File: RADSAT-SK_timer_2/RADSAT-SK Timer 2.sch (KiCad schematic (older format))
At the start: 54 parts, among them J201 Conn_01x07, J202 Conn_01x05_Female, J203 Conn_01x03, J204 Conn_01x02, J205 Conn_01x02, J206 Conn_01x02, J207 Conn_02x26_Odd_Even, J208 Conn_02x26_Odd_Even, J209 Conn_01x15, Q101 IRLML2060, Q102 IRLML2060, Q103 IRLML2060, SW201 SW_Push, SW202 SW_Push, SW203 SW_Push, SW204 SW_Push, SW205 SW_Push, SW206 SW_Push, U101 LT1521IS8-5TR, U202 TPS3700DDCR, U230 CPC1114N, U240 CPC1114N, U250 CPC1114N, U260 CPC1114N

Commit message: added test points
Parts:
- removed J209: Conn_01x15, Connector_Hirose:Hirose_DF13-15P-1.25DSA_1x15_P1.25mm_Vertical, symbol Connector_Generic:Conn_01x15
- added TP101, TP102, TP103, TP104, TP105, TP106, TP107, TP108, TP109, TP110, TP111, TP112, TP113, TP114, TP115, TP116: TestPoint, S2761-46R:HARWIN_S2761-46R, symbol Connector:TestPoint
- C103: value C -> 10uF
- R103: value R -> 1k
- R104: value R -> 2k
- renumbered Q101 to Q204, Q103 to Q205, Q102 to Q206
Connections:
- net labels removed: Test_CHRG_ON-OFF, Test_CSKB_3V3, Test_CSKB_5V, Test_GND, Test_I2C_CLK, Test_I2C_DATA, Test_INA+, Test_INB-, Test_InhibV+, Test_Relay_Inhibs, Test_SW1, Test_SW2, Test_USB_Charge, Test_Vreg, Test_negetive_Batt
- wire segments 185 -> 194

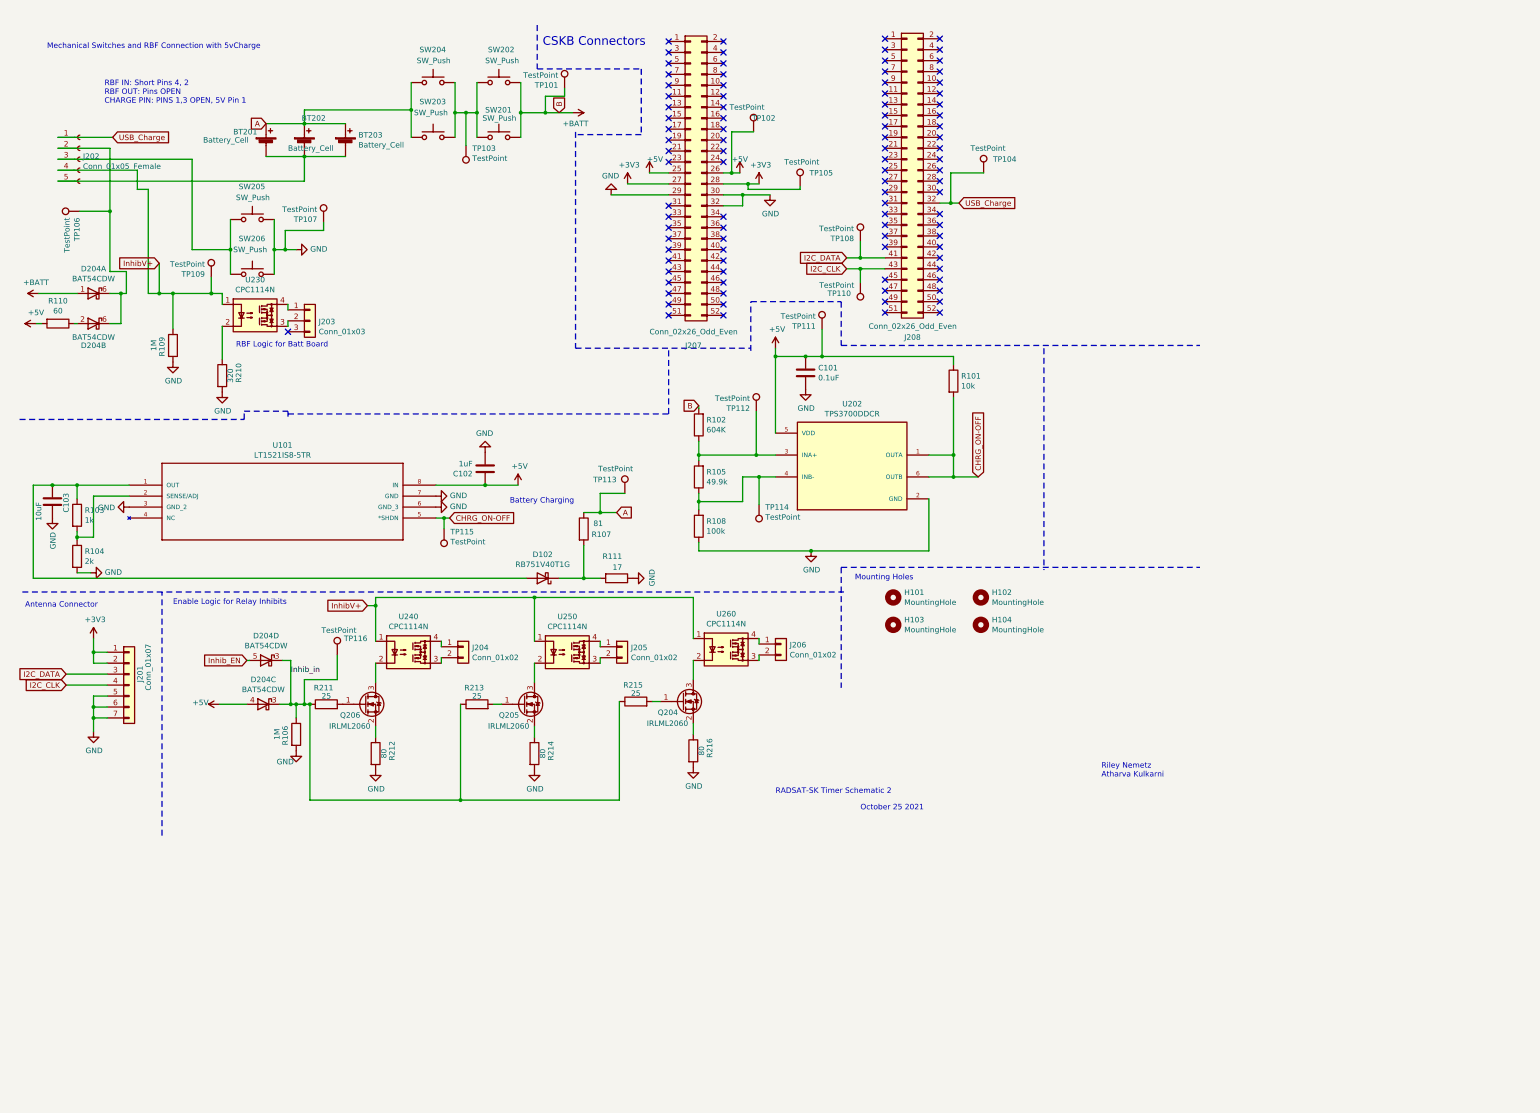
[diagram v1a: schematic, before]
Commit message: added galaxia timer in schematic, made footprint for galaxia timer and added to PCB new
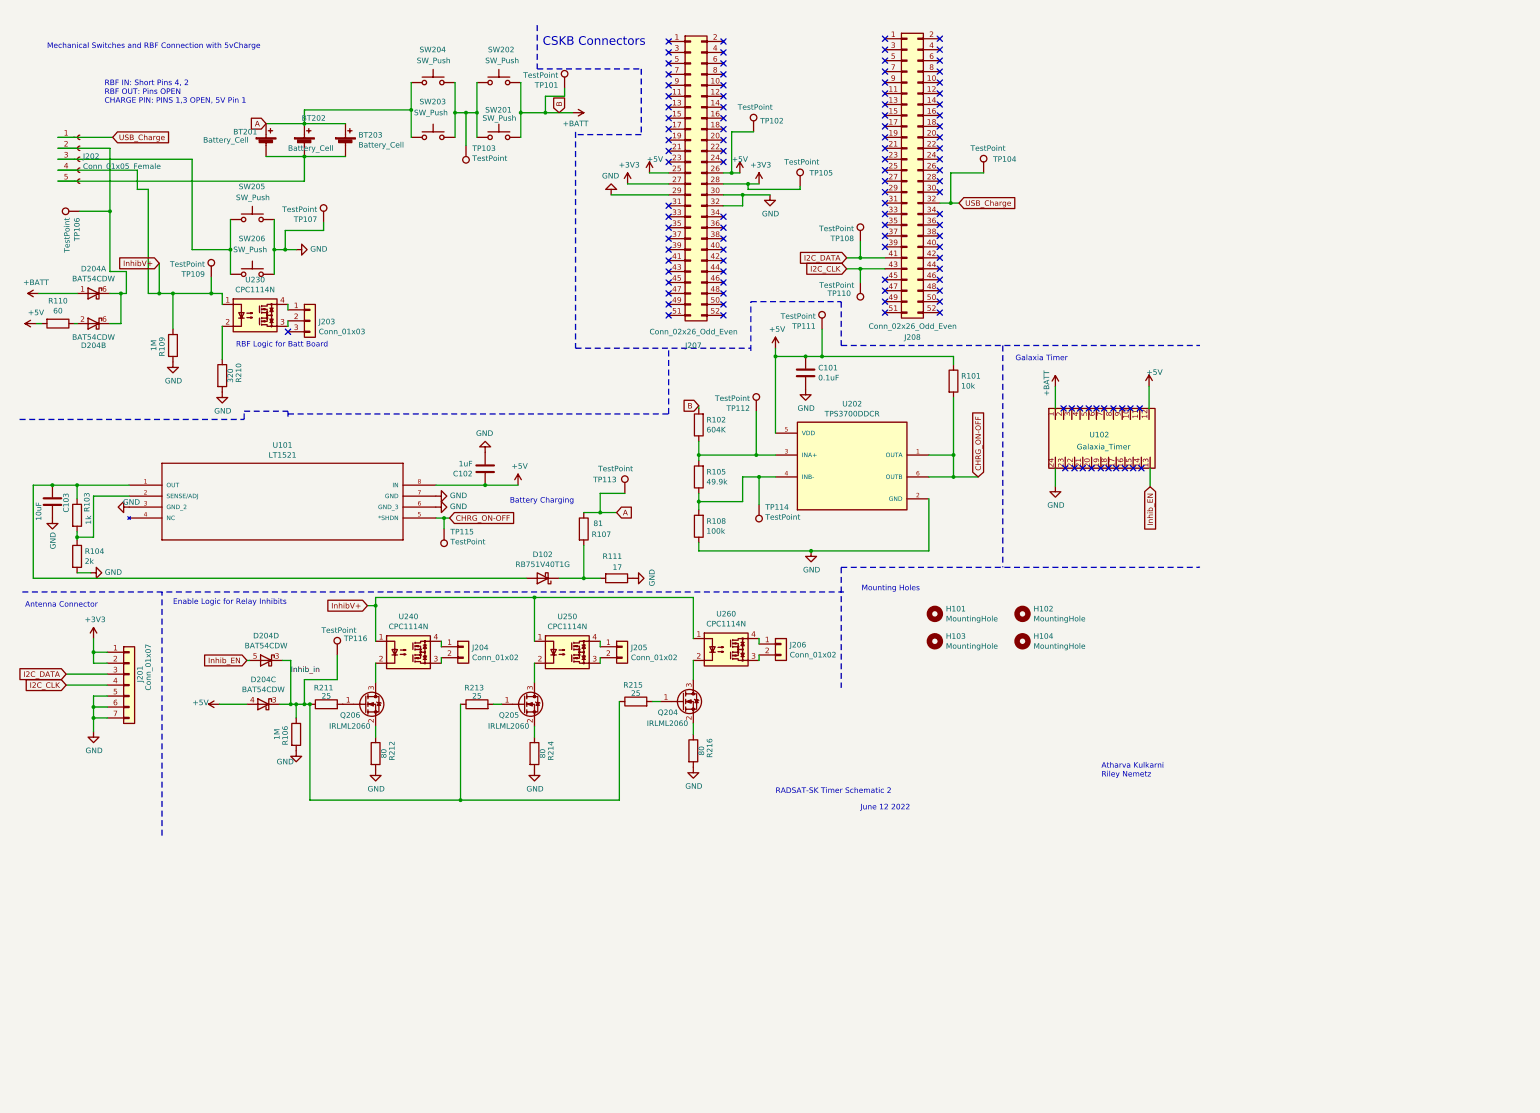
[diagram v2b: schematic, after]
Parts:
- added U102: Galaxia_Timer, Galaxia_Timer:Galaxia_Timer, symbol Galaxia_Timer:Galaxia_Timer
- U101: value LT1521IS8-5TR -> LT1521
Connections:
- net +5V: now also U102.12
- net +BATT: now also U102.1
- net GND: now also U102.24
- net Inhib_EN: now also U102.13
- no-connect marks 95 -> 115
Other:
- note added: "Atharva Kulkarni\nRiley Nemetz\n"
- note added: "Galaxia Timer\n"
- note added: "June 12 2022"
- note removed: "October 25 2021"
- note removed: "Riley Nemetz\nAtharva Kulkarni"
- moved on the sheet: H101, H102, H103, H104
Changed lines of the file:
@@
 Comment4 ""
 $EndDescr
-Text Notes 10325 7350 0    50   ~ 0
-Riley Nemetz\nAtharva Kulkarni
 Text Notes 700  700  0    50   ~ 0
 Mechanical Switches and RBF Connection with 5vCharge
@@
 $EndComp
 Text Notes 8125 7650 0    50   ~ 0
-October 25 2021
+June 12 2022
 $Comp
 L BAT54CDW:BAT54CDW D204
@@
 L Mechanical:MountingHole H101
 U 1 1 62BD786D
-P 8425 5700
+P 8805 5850
 AR Path="/62BD786D" Ref="H101"  Part="1"
 AR Path="/602E25D3/62BD786D" Ref="H101"  Part="1"
-F 0 "H101" H 8525 5746 50  0000 L CNN
-F 1 "MountingHole" H 8525 5655 50  0000 L CNN
-F 2 "MountingHole:MountingHole_3.2mm_M3_ISO7380_Pad_TopBottom" H 8425 5700 50  0001 C CNN
-F 3 "~" H 8425 5700 50  0001 C CNN
-	1    8425 5700
+F 0 "H101" H 8905 5896 50  0000 L CNN
+F 1 "MountingHole" H 8905 5805 50  0000 L CNN
+F 2 "MountingHole:MountingHole_3.2mm_M3_ISO7380_Pad_TopBottom" H 8805 5850 50  0001 C CNN
+F 3 "~" H 8805 5850 50  0001 C CNN
+	1    8805 5850
 	1    0    0    -1
 $EndComp
@@
 L Mechanical:MountingHole H103
 U 1 1 62BD7873
-P 8425 5950
+P 8805 6100
 AR Path="/62BD7873" Ref="H103"  Part="1"
 AR Path="/602E25D3/62BD7873" Ref="H102"  Part="1"
-F 0 "H103" H 8525 5996 50  0000 L CNN
-F 1 "MountingHole" H 8525 5905 50  0000 L CNN
-F 2 "MountingHole:MountingHole_3.2mm_M3_ISO7380_Pad_TopBottom" H 8425 5950 50  0001 C CNN
-F 3 "~" H 8425 5950 50  0001 C CNN
-	1    8425 5950
+F 0 "H103" H 8905 6146 50  0000 L CNN
+F 1 "MountingHole" H 8905 6055 50  0000 L CNN
+F 2 "MountingHole:MountingHole_3.2mm_M3_ISO7380_Pad_TopBottom" H 8805 6100 50  0001 C CNN
+F 3 "~" H 8805 6100 50  0001 C CNN
+	1    8805 6100
 	1    0    0    -1
 $EndComp
@@
 L Mechanical:MountingHole H104
 U 1 1 62BD7879
-P 9225 5950
+P 9605 6100
 AR Path="/62BD7879" Ref="H104"  Part="1"
 AR Path="/602E25D3/62BD7879" Ref="H104"  Part="1"
-F 0 "H104" H 9325 5996 50  0000 L CNN
-F 1 "MountingHole" H 9325 5905 50  0000 L CNN
-F 2 "MountingHole:MountingHole_3.2mm_M3_ISO7380_Pad_TopBottom" H 9225 5950 50  0001 C CNN
-F 3 "~" H 9225 5950 50  0001 C CNN
-	1    9225 5950
+F 0 "H104" H 9705 6146 50  0000 L CNN
+F 1 "MountingHole" H 9705 6055 50  0000 L CNN
+F 2 "MountingHole:MountingHole_3.2mm_M3_ISO7380_Pad_TopBottom" H 9605 6100 50  0001 C CNN
+F 3 "~" H 9605 6100 50  0001 C CNN
+	1    9605 6100
 	1    0    0    -1
 $EndComp
@@
 L Mechanical:MountingHole H102
 U 1 1 62BD787F
-P 9225 5700
+P 9605 5850
 AR Path="/62BD787F" Ref="H102"  Part="1"
 AR Path="/602E25D3/62BD787F" Ref="H103"  Part="1"
-F 0 "H102" H 9325 5746 50  0000 L CNN
-F 1 "MountingHole" H 9325 5655 50  0000 L CNN
-F 2 "MountingHole:MountingHole_3.2mm_M3_ISO7380_Pad_TopBottom" H 9225 5700 50  0001 C CNN
-F 3 "~" H 9225 5700 50  0001 C CNN
-	1    9225 5700
+F 0 "H102" H 9705 5896 50  0000 L CNN
+F 1 "MountingHole" H 9705 5805 50  0000 L CNN
+F 2 "MountingHole:MountingHole_3.2mm_M3_ISO7380_Pad_TopBottom" H 9605 5850 50  0001 C CNN
+F 3 "~" H 9605 5850 50  0001 C CNN
+	1    9605 5850
 	1    0    0    -1
 $EndComp
 Wire Notes Line
 	7950 5425 7950 6525
-Text Notes 8075 5550 0    50   ~ 0
+Text Notes 8135 5650 0    50   ~ 0
 Mounting Holes\n
 Wire Wire Line
@@
 Wire Wire Line
 	1725 2925 1850 2925
-Wire Notes Line
-	9800 3425 9800 5450
-Wire Notes Line
-	7950 5425 11225 5425
 $Comp
 L Device:R R106
@@
 AR Path="/62B5231F" Ref="U101"  Part="1"
 F 0 "U101" H 2850 5040 50  0000 C CNN
-F 1 "LT1521IS8-5TR" H 2850 4949 50  0000 C CNN
+F 1 "LT1521" H 2850 4949 50  0000 C CNN
 F 2 "LT1521IS8-5TR:SO-8_S" H 1450 4675 50  0001 L BNN
 F 3 "" H 1450 4675 50  0001 L BNN
@@
 U 1 1 62C899A2
 P 975 4950
-F 0 "R103" H 1045 4996 50  0000 L CNN
-F 1 "1k" H 1045 4905 50  0000 L CNN
+F 0 "R103" V 1065 4980 50  0000 L CNN
+F 1 "1k" V 1080 4865 50  0000 L CNN
 F 2 "Resistor_SMD:R_0805_2012Metric" V 905 4950 50  0001 C CNN
 F 3 "~" H 975 4950 50  0001 C CNN
@@
 P 1450 4875
 F 0 "#PWR0111" H 1450 4625 50  0001 C CNN
-F 1 "GND" V 1455 4747 50  0000 R CNN
+F 1 "GND" V 1405 4975 50  0000 R CNN
 F 2 "" H 1450 4875 50  0001 C CNN
 F 3 "" H 1450 4875 50  0001 C CNN
@@
 U 1 1 62C49D73
 P 7150 1450
-F 0 "TP102" H 7350 1575 50  0000 R CNN
-F 1 "TestPoint" H 7250 1675 50  0000 R CNN
+F 0 "TP102" H 7425 1550 50  0000 R CNN
+F 1 "TestPoint" H 7325 1675 50  0000 R CNN
 F 2 "S2761-46R:HARWIN_S2761-46R" H 7350 1450 50  0001 C CNN
 F 3 "~" H 7350 1450 50  0001 C CNN
@@
 	1    0    0    -1
 $EndComp
+Text Notes 10325 7350 0    50   ~ 0
+Atharva Kulkarni\nRiley Nemetz\n
+Wire Notes Line
+	9425 3400 9425 5425
+$Comp
+L Galaxia_Timer:Galaxia_Timer U102
+U 1 1 62C45797
+P 10400 4075
+F 0 "U102" H 10215 3935 50  0000 L CNN
+F 1 "Galaxia_Timer" H 10100 3825 50  0000 L CNN
+F 2 "Galaxia_Timer:Galaxia_Timer" H 10400 4070 50  0001 C CNN
+F 3 "" H 10400 4070 50  0001 C CNN
+	1    10400 4075
+	1    0    0    -1
+$EndComp
+Wire Wire Line
+	9905 3975 9905 3775
+$Comp
+L power:+BATT #PWR0129
+U 1 1 62C47EA6
+P 9905 3775
+F 0 "#PWR0129" H 9905 3625 50  0001 C CNN
+F 1 "+BATT" V 9825 3805 50  0000 C CNN
+F 2 "" H 9905 3775 50  0001 C CNN
+F 3 "" H 9905 3775 50  0001 C CNN
+	1    9905 3775
+	1    0    0    -1
+$EndComp
+Wire Wire Line
+	10760 3975 10760 3770
+$Comp
+L power:+5V #PWR0130
+U 1 1 62CA2DBB
+P 10760 3770
+AR Path="/62CA2DBB" Ref="#PWR0130"  Part="1"
+AR Path="/602E25D3/62CA2DBB" Ref="#PWR?"  Part="1"
+F 0 "#PWR0130" H 10760 3620 50  0001 C CNN
+F 1 "+5V" H 10810 3895 50  0000 C CNN
+F 2 "" H 10760 3770 50  0001 C CNN
+F 3 "" H 10760 3770 50  0001 C CNN
+	1    10760 3770
+	1    0    0    -1
+$EndComp
+Text GLabel 10770 4690 3    50   Input ~ 0
+Inhib_EN
+Wire Wire Line
+	10770 4520 10770 4690
+Wire Wire Line
+	9905 4520 9905 4685
+$Comp
+L power:GND #PWR0131
+U 1 1 62D1A3FF
+P 9905 4685
+F 0 "#PWR0131" H 9905 4435 50  0001 C CNN
+F 1 "GND" H 9910 4512 50  0000 C CNN
+F 2 "" H 9905 4685 50  0001 C CNN
+F 3 "" H 9905 4685 50  0001 C CNN
+	1    9905 4685
+	1    0    0    -1
+$EndComp
+NoConn ~ 9980 3975
+NoConn ~ 10055 3975
+NoConn ~ 10130 3975
+NoConn ~ 10210 3975
+NoConn ~ 10280 3975
+NoConn ~ 10350 3975
+NoConn ~ 10435 3975
+NoConn ~ 10515 3975
+NoConn ~ 10590 3975
+NoConn ~ 10675 3975
+NoConn ~ 9995 4520
+NoConn ~ 10080 4520
+NoConn ~ 10155 4520
+NoConn ~ 10235 4520
+NoConn ~ 10320 4520
+NoConn ~ 10390 4520
+NoConn ~ 10460 4520
+NoConn ~ 10540 4520
+NoConn ~ 10615 4520
+NoConn ~ 10690 4520
+Text Notes 9540 3550 0    50   ~ 0
+Galaxia Timer\n
+Wire Notes Line
+	11220 5425 11220 5420
+Wire Notes Line
+	7950 5425 11220 5425
 $EndSCHEMATC
